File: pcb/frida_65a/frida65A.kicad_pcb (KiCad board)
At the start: 2 copper layers, 60 x 60 mm, 35 parts, among them J10 TP_LOGIC, J11 TP_OUT, J2 CONN_IN_P, J4 TP_CFG, J5 CONN_CFG, J6 TP_IN, J7 TP_INIT, J8 TP_SAMP, J9 TP_COMP, U1 DUT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

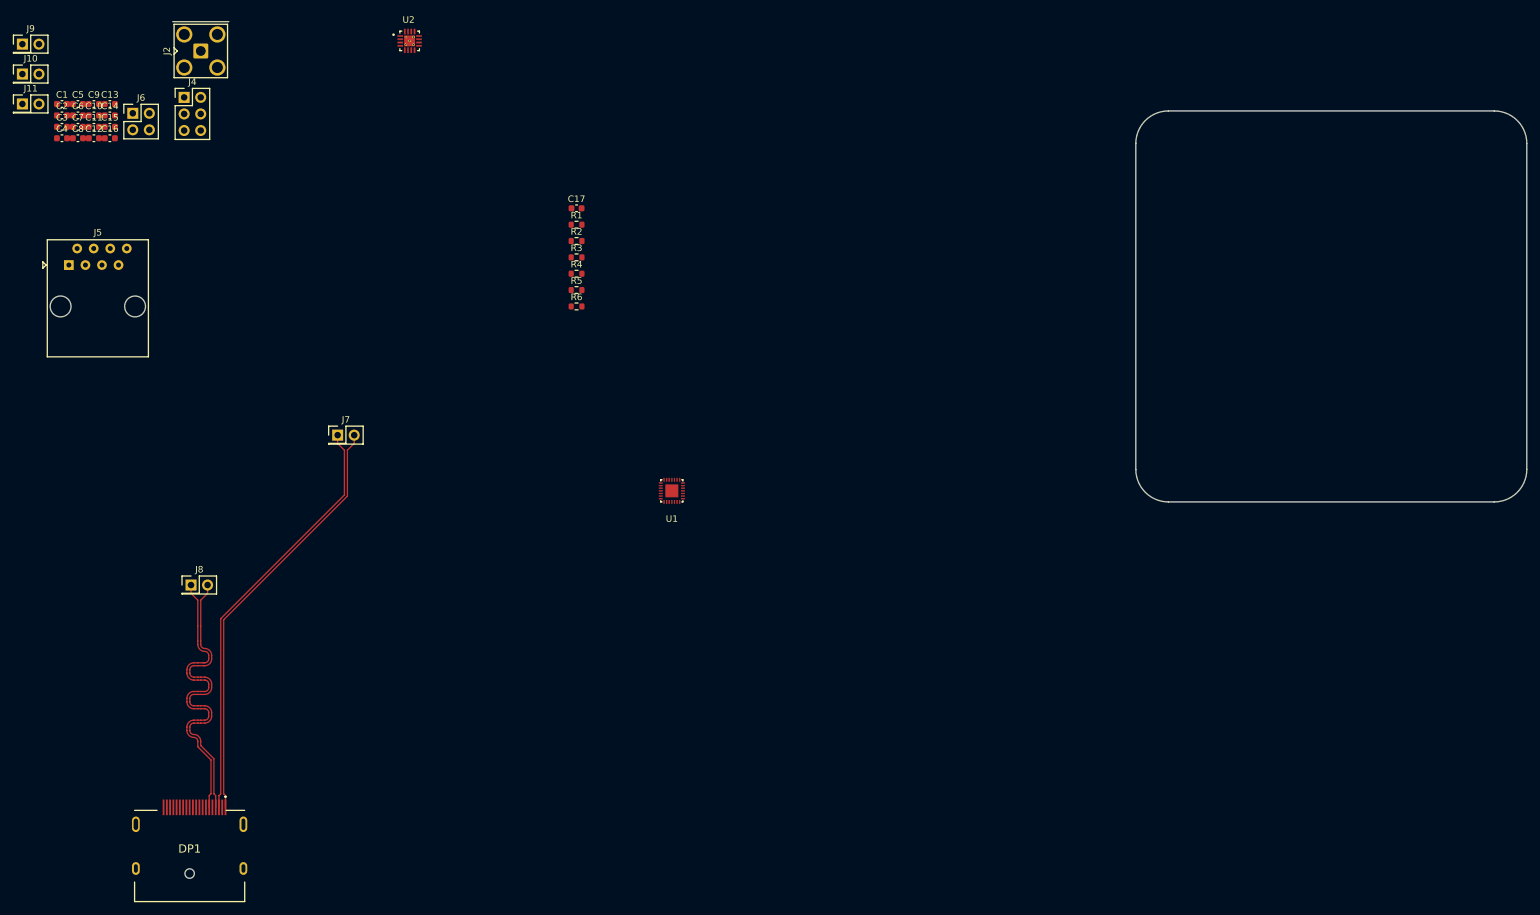
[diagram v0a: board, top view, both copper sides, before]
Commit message: Replace PostEvaluator with direct pickle loading so our expression functions actually work
- Load .pck files directly and inject flow.expression as 'm' into eval environment
- Auto-detect local vs remote for make sim (no more host= parameter)
- Add checks for spectre/lmstat in PATH before trying to simulate
- Suppress matplotlib font manager spam in logs
- PCB and OpenROAD stage updates
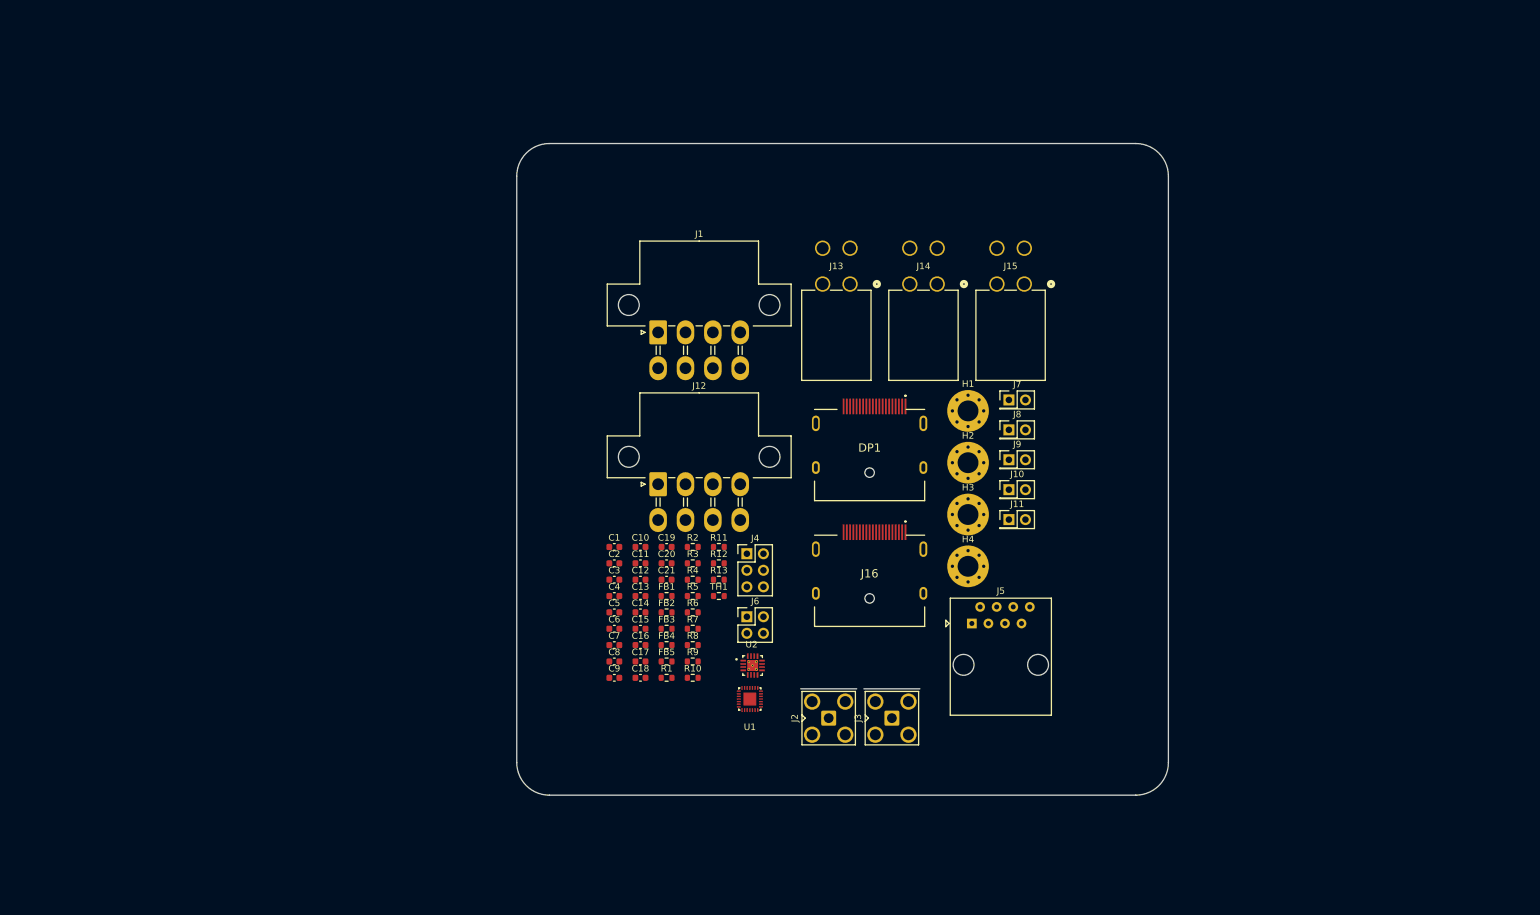
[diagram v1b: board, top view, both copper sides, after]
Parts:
- added C18: 47u, Capacitor_SMD:C_0603_1608Metric, F.Cu at (119.0, 132.0)
- added C19: 1u, Capacitor_SMD:C_0603_1608Metric, F.Cu at (123.0, 111.9)
- added C20: 100n, Capacitor_SMD:C_0603_1608Metric, F.Cu at (123.0, 114.4)
- added C21: 100n, Capacitor_SMD:C_0603_1608Metric, F.Cu at (123.0, 116.9)
- added FB1: FerriteBead_Small, Resistor_SMD:R_0603_1608Metric, F.Cu at (123.0, 119.4)
- added FB2: FerriteBead_Small, Resistor_SMD:R_0603_1608Metric, F.Cu at (123.0, 122.0)
- added FB3: FerriteBead_Small, Resistor_SMD:R_0603_1608Metric, F.Cu at (123.0, 124.5)
- added FB4: FerriteBead_Small, Resistor_SMD:R_0603_1608Metric, F.Cu at (123.0, 127.0)
- added FB5: FerriteBead_Small, Resistor_SMD:R_0603_1608Metric, F.Cu at (123.0, 129.5)
- added H1: MountingHole_Pad, MountingHole:MountingHole_3.2mm_M3_Pad_Via, F.Cu at (169.3, 91.0)
- added H2: MountingHole_Pad, MountingHole:MountingHole_3.2mm_M3_Pad_Via, F.Cu at (169.3, 99.0)
- added H3: MountingHole_Pad, MountingHole:MountingHole_3.2mm_M3_Pad_Via, F.Cu at (169.3, 106.9)
- added H4: MountingHole_Pad, MountingHole:MountingHole_3.2mm_M3_Pad_Via, F.Cu at (169.3, 114.9)
- added J1: TP_PWR, frida65A:Molex_Mini-Fit_Jr_5569-08A1_2x04_P4.20mm_Horizontal, F.Cu at (121.7, 79.0)
- added J12: J_P, frida65A:Molex_Mini-Fit_Jr_5569-08A1_2x04_P4.20mm_Horizontal, F.Cu at (121.7, 102.3)
- added J13: 469914004, frida65A:CONN_SD-46991-001_04_MOL, F.Cu at (151.1, 71.6)
- added J14: 469914004, frida65A:CONN_SD-46991-001_04_MOL, F.Cu at (164.5, 71.6)
- added J15: 469914004, frida65A:CONN_SD-46991-001_04_MOL, F.Cu at (177.9, 71.6)
- added J16: J_N, frida65A:displayport, F.Cu at (154.2, 116.0)
- added J3: CONN_IN_N, Connector_Coaxial:SMA_Amphenol_901-143_Horizontal, F.Cu at (157.6, 138.2)
- added R10: 10k, Resistor_SMD:R_0603_1608Metric, F.Cu at (127.0, 132.0)
- added R11: 10k, Resistor_SMD:R_0603_1608Metric, F.Cu at (131.0, 111.9)
- added R12: 10k, Resistor_SMD:R_0603_1608Metric, F.Cu at (131.0, 114.4)
- added R13: 10k, Resistor_SMD:R_0603_1608Metric, F.Cu at (131.0, 116.9)
- added R7: 10k, Resistor_SMD:R_0603_1608Metric, F.Cu at (127.0, 124.5)
- added R8: 10k, Resistor_SMD:R_0603_1608Metric, F.Cu at (127.0, 127.0)
- added R9: 10k, Resistor_SMD:R_0603_1608Metric, F.Cu at (127.0, 129.5)
- added TH1: Thermistor_NTC, Resistor_SMD:R_0603_1608Metric, F.Cu at (131.0, 119.4)
- DP1: footprint silab:DP_Molex_47272-0024 -> frida65A:displayport
- R5: value 100 -> 10k
- moved J10 164.3 mm to (175.5, 103.1)
- moved J11 164.3 mm to (175.5, 107.7)
- moved J9 164.3 mm to (175.5, 98.5)
- moved J5 149.1 mm to (169.8, 123.7)
- moved J2 140.6 mm to (147.9, 138.2)
- moved J8 127.8 mm to (175.5, 93.9)
- moved J6 121.9 mm to (135.3, 122.6)
- moved DP1 121.1 mm to (154.2, 96.7)
- moved C9 118.9 mm to (115.0, 132.0)
- moved C8 115.0 mm to (115.0, 129.5)
- moved C7 114.5 mm to (115.0, 127.0)
- moved C6 113.9 mm to (115.0, 124.5)
- moved C5 113.4 mm to (115.0, 122.0)
- moved C16 112.6 mm to (119.0, 127.0)
- moved C15 112.1 mm to (119.0, 124.5)
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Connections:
- DP1 pad 1: /CLK_INIT_N -> /CLK_LOGIC_N
- DP1 pad 10: /CLK_LOGIC_N -> /CLK_INIT_N
- DP1 pad 12: /CLK_LOGIC_P -> /CLK_INIT_P
- DP1 pad 13: unconnected-(DP1-Pad13) -> Net-(DP1-Pad13)
- DP1 pad 14: unconnected-(DP1-Pad14) -> Net-(DP1-Pad14)
- DP1 pad 15: /COMP_OUT_N -> /COMP_OUT_P
- DP1 pad 17: /COMP_OUT_P -> /COMP_OUT_N
- DP1 pad 19: unconnected-(DP1-Pad19) -> /VDD_IO
- DP1 pad 3: /CLK_INIT_P -> /CLK_LOGIC_P
- DP1 pad 4: /CLK_SAMP_N -> /CLK_COMP_N
- DP1 pad 6: /CLK_SAMP_P -> /CLK_COMP_P
- DP1 pad 7: /CLK_COMP_N -> /CLK_SAMP_N
- DP1 pad 9: /CLK_COMP_P -> /CLK_SAMP_P
- J11 pad 1: /COMP_OUT_P -> /COMP_OUT_N
- J11 pad 2: /COMP_OUT_N -> /COMP_OUT_P
- J2 pad 1: Net-(J2-In) -> /VIN_P_EXT
- J6 pad 1: Net-(J2-In) -> Net-(J12-Pin_3)
- R1 pad 1: /CLK_INIT_N -> /CLK_LOGIC_N
- R1 pad 2: /CLK_INIT_P -> /CLK_LOGIC_P
- R2 pad 1: /CLK_SAMP_N -> /CLK_COMP_N
- R2 pad 2: /CLK_SAMP_P -> /CLK_COMP_P
- R3 pad 1: /CLK_COMP_N -> /CLK_SAMP_N
- R3 pad 2: /CLK_COMP_P -> /CLK_SAMP_P
- R4 pad 1: /CLK_LOGIC_N -> /CLK_INIT_N
- R4 pad 2: /CLK_LOGIC_P -> /CLK_INIT_P
- R5 pad 1: /COMP_OUT_N -> /CLK_INIT_P
- R5 pad 2: /COMP_OUT_P -> GND
- R6 pad 1: Earth -> /CLK_INIT_N
- U1 pad 25: Net-(J2-In) -> Net-(J12-Pin_3)
- U2 pad 10: unconnected-(U2-VOUT--Pad10) -> Net-(J16-Pin_1)
- U2 pad 13: unconnected-(U2-VS--Pad13) -> GND
- U2 pad 14: unconnected-(U2-VS-__1-Pad14) -> GND
- U2 pad 15: unconnected-(U2-VS-__2-Pad15) -> GND
- U2 pad 16: unconnected-(U2-VS-__3-Pad16) -> GND
- U2 pad 17: unconnected-(U2-EP-Pad17) -> GND
- U2 pad 3: unconnected-(U2-VOUT+-Pad3) -> Net-(J12-Pin_1)
- U2 pad 5: unconnected-(U2-VS+-Pad5) -> /VDD_DIF
- U2 pad 6: unconnected-(U2-VS+__1-Pad6) -> /VDD_DIF
- U2 pad 7: unconnected-(U2-VS+__2-Pad7) -> /VDD_DIF
- U2 pad 8: unconnected-(U2-VS+__3-Pad8) -> /VDD_DIF
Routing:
- net /CLK_INIT_P: track 65.5 -> 0.00 mm
- net /CLK_INIT_N: track 65.5 -> 0.00 mm
- net /CLK_SAMP_N: track 50.1 -> 0.00 mm
- net /CLK_SAMP_P: track 50.1 -> 0.00 mm
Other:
- board size 60 x 60 mm -> 100 x 100 mm
